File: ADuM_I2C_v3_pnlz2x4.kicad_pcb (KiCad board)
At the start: 4 copper layers, 50 x 50 mm, 336 parts, among them J1 A, J2 B, Q1 BSS138, Q2 BSS138, Q3 BSS138, Q4 BSS138, Q5 BSS138, Q6 BSS138, Q7 BSS138, Q8 BSS138, U1 ADuM1251ARZ, U2 ADuM1201AR

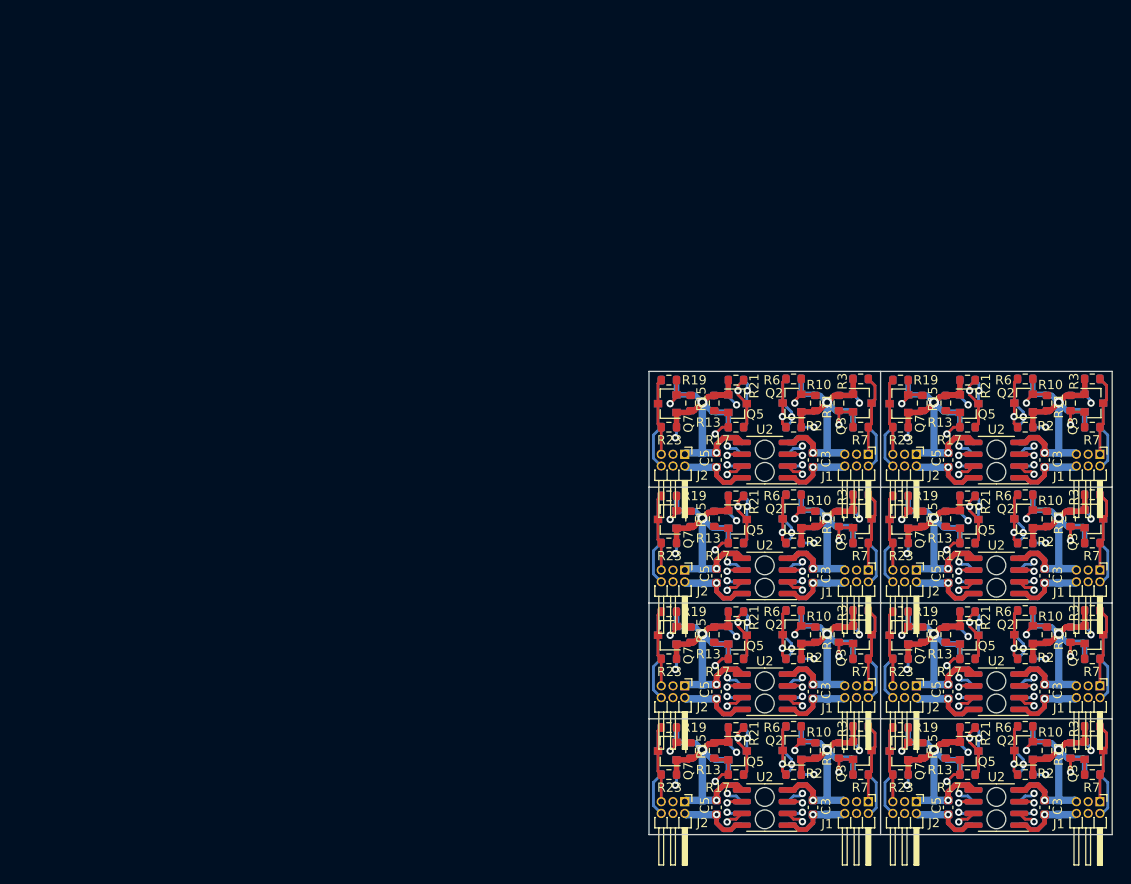
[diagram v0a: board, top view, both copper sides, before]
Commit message: Переделана панелизация платы ADuM_I2C_v3
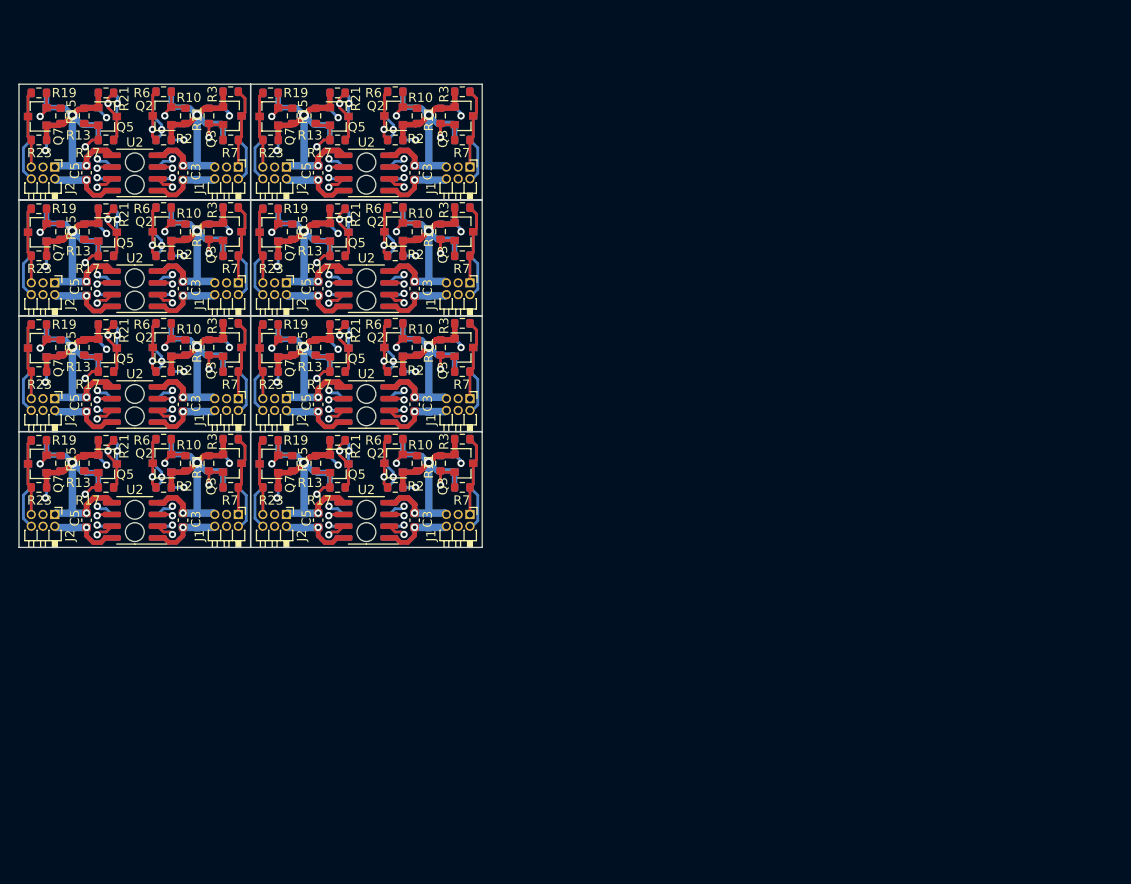
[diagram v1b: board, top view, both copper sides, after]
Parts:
- removed the C1 at (161.7, 126.6)
- removed the C1 at (136.7, 126.6)
- removed the C1 at (161.7, 114.1)
- removed the C1 at (136.7, 114.1)
- removed the C1 at (161.7, 101.6)
- removed the C1 at (136.7, 101.6)
- removed the C1 at (161.7, 89.1)
- removed the C2 at (160.2, 126.6)
- removed the C2 at (135.2, 126.6)
- removed the C2 at (160.2, 114.1)
- removed the C2 at (135.2, 114.1)
- removed the C2 at (160.2, 101.6)
- removed the C2 at (135.2, 101.6)
- removed the C2 at (160.2, 89.1)
- removed the C3 at (160.2, 126.6)
- removed the C3 at (135.2, 126.6)
- removed the C3 at (160.2, 114.1)
- removed the C3 at (135.2, 114.1)
- removed the C3 at (160.2, 101.6)
- removed the C3 at (135.2, 101.6)
- removed the C3 at (160.2, 89.1)
- removed the C4 at (149.8, 126.6)
- removed the C4 at (124.8, 126.6)
- removed the C4 at (149.8, 114.1)
- removed the C4 at (124.8, 114.1)
- removed the C4 at (149.8, 101.6)
- removed the C4 at (124.8, 101.6)
- removed the C4 at (149.8, 89.1)
- removed the C5 at (149.8, 126.6)
- removed the C5 at (124.8, 126.6)
- removed the C5 at (149.8, 114.1)
- removed the C5 at (124.8, 114.1)
- removed the C5 at (149.8, 101.6)
- removed the C5 at (124.8, 101.6)
- removed the C5 at (149.8, 89.1)
- removed the C6 at (148.3, 126.6)
- removed the C6 at (123.3, 126.6)
- removed the C6 at (148.3, 114.1)
- removed the C6 at (123.3, 114.1)
- removed the C6 at (148.3, 101.6)
- removed the C6 at (123.3, 101.6)
- removed the C6 at (148.3, 89.1)
- removed the J1 at (166.2, 125.9)
- removed the J1 at (141.2, 125.9)
- removed the J1 at (166.2, 113.4)
- removed the J1 at (141.2, 113.4)
- removed the J1 at (166.2, 100.9)
- removed the J1 at (141.2, 100.9)
- removed the J1 at (166.2, 88.4)
- removed the J2 at (146.4, 125.9)
- removed the J2 at (121.4, 125.9)
- removed the J2 at (146.4, 113.4)
- removed the J2 at (121.4, 113.4)
- removed the J2 at (146.4, 100.9)
- removed the J2 at (121.4, 100.9)
- removed the J2 at (146.4, 88.4)
- removed the Q1 at (157.9, 120.4)
- removed the Q1 at (132.9, 120.4)
- removed the Q1 at (157.9, 107.9)
- removed the Q1 at (132.9, 107.9)
- removed the Q1 at (157.9, 95.4)
- removed the Q1 at (132.9, 95.4)
- removed the Q1 at (157.9, 82.9)
- removed the Q2 at (157.9, 120.4)
- removed the Q2 at (132.9, 120.4)
- removed the Q2 at (157.9, 107.9)
- removed the Q2 at (132.9, 107.9)
- removed the Q2 at (157.9, 95.4)
- removed the Q2 at (132.9, 95.4)
- removed the Q2 at (157.9, 82.9)
- removed the Q3 at (165.5, 120.4)
- removed the Q3 at (140.5, 120.4)
- removed the Q3 at (165.5, 107.9)
- removed the Q3 at (140.5, 107.9)
- removed the Q3 at (165.5, 95.4)
- removed the Q3 at (140.5, 95.4)
- removed the Q3 at (165.5, 82.9)
- removed the Q4 at (165.5, 120.4)
- removed the Q4 at (140.5, 120.4)
- removed the Q4 at (165.5, 107.9)
- removed the Q4 at (140.5, 107.9)
- removed the Q4 at (165.5, 95.4)
- removed the Q4 at (140.5, 95.4)
- removed the Q4 at (165.5, 82.9)
- removed the Q5 at (152.1, 120.5)
- removed the Q5 at (127.1, 120.5)
- removed the Q5 at (152.1, 108.0)
- removed the Q5 at (127.1, 108.0)
- removed the Q5 at (152.1, 95.5)
- removed the Q5 at (127.1, 95.5)
- removed the Q5 at (152.1, 83.0)
- removed the Q6 at (152.1, 120.5)
- removed the Q6 at (127.1, 120.5)
- removed the Q6 at (152.1, 108.0)
- removed the Q6 at (127.1, 108.0)
- removed the Q6 at (152.1, 95.5)
- removed the Q6 at (127.1, 95.5)
- removed the Q6 at (152.1, 83.0)
- removed the Q7 at (144.5, 120.5)
- removed the Q7 at (119.5, 120.5)
- removed the Q7 at (144.5, 108.0)
- removed the Q7 at (119.5, 108.0)
- removed the Q7 at (144.5, 95.5)
- removed the Q7 at (119.5, 95.5)
- removed the Q7 at (144.5, 83.0)
- removed the Q8 at (144.5, 120.5)
- removed the Q8 at (119.5, 120.5)
- removed the Q8 at (144.5, 108.0)
- removed the Q8 at (119.5, 108.0)
- removed the Q8 at (144.5, 95.5)
- removed the Q8 at (119.5, 95.5)
- removed the Q8 at (144.5, 83.0)
- removed the R1 at (158.1, 117.8)
- removed the R1 at (133.1, 117.8)
- removed the R1 at (158.1, 105.3)
- removed the R1 at (133.1, 105.3)
- removed the R1 at (158.1, 92.8)
- removed the R1 at (133.1, 92.8)
- removed the R1 at (158.1, 80.3)
- removed the R10 at (160.5, 120.4)
- removed the R10 at (135.5, 120.4)
- removed the R10 at (160.5, 107.9)
- removed the R10 at (135.5, 107.9)
- removed the R10 at (160.5, 95.4)
- removed the R10 at (135.5, 95.4)
- removed the R10 at (160.5, 82.9)
- removed the R11 at (163.0, 120.4)
- removed the R11 at (138.0, 120.4)
- removed the R11 at (163.0, 107.9)
- removed the R11 at (138.0, 107.9)
- removed the R11 at (163.0, 95.4)
- removed the R11 at (138.0, 95.4)
- removed the R11 at (163.0, 82.9)
- removed the R12 at (163.0, 120.4)
- removed the R12 at (138.0, 120.4)
- removed the R12 at (163.0, 107.9)
- removed the R12 at (138.0, 107.9)
- removed the R12 at (163.0, 95.4)
- removed the R12 at (138.0, 95.4)
- removed the R12 at (163.0, 82.9)
- removed the R13 at (149.5, 120.4)
- removed the R13 at (124.5, 120.4)
- removed the R13 at (149.5, 107.9)
- removed the R13 at (124.5, 107.9)
- removed the R13 at (149.5, 95.4)
- removed the R13 at (124.5, 95.4)
- removed the R13 at (149.5, 82.9)
- removed the R14 at (149.5, 120.4)
- removed the R14 at (124.5, 120.4)
- removed the R14 at (149.5, 107.9)
- removed the R14 at (124.5, 107.9)
- removed the R14 at (149.5, 95.4)
- removed the R14 at (124.5, 95.4)
- removed the R14 at (149.5, 82.9)
- removed the R15 at (147.0, 120.4)
- removed the R15 at (122.0, 120.4)
- removed the R15 at (147.0, 107.9)
- removed the R15 at (122.0, 107.9)
- removed the R15 at (147.0, 95.4)
- removed the R15 at (122.0, 95.4)
- removed the R15 at (147.0, 82.9)
- removed the R16 at (147.0, 120.4)
- removed the R16 at (122.0, 120.4)
- removed the R16 at (147.0, 107.9)
- removed the R16 at (122.0, 107.9)
- removed the R16 at (147.0, 95.4)
- removed the R16 at (122.0, 95.4)
- removed the R16 at (147.0, 82.9)
- removed the R17 at (151.9, 123.0)
- removed the R17 at (126.9, 123.0)
- removed the R17 at (151.9, 110.5)
- removed the R17 at (126.9, 110.5)
- removed the R17 at (151.9, 98.0)
- removed the R17 at (126.9, 98.0)
- removed the R17 at (151.9, 85.5)
- removed the R18 at (151.9, 117.9)
- removed the R18 at (126.9, 117.9)
- removed the R18 at (151.9, 105.4)
- removed the R18 at (126.9, 105.4)
- removed the R18 at (151.9, 92.9)
- removed the R18 at (126.9, 92.9)
- removed the R18 at (151.9, 80.4)
- removed the R19 at (144.6, 117.9)
- removed the R19 at (119.6, 117.9)
- removed the R19 at (144.6, 105.4)
- removed the R19 at (119.6, 105.4)
- removed the R19 at (144.6, 92.9)
- removed the R19 at (119.6, 92.9)
- removed the R19 at (144.6, 80.4)
- removed the R2 at (158.1, 123.0)
- removed the R2 at (133.1, 123.0)
- removed the R2 at (158.1, 110.5)
- removed the R2 at (133.1, 110.5)
- removed the R2 at (158.1, 98.0)
- removed the R2 at (133.1, 98.0)
- removed the R2 at (158.1, 85.5)
- removed the R20 at (144.7, 123.0)
- removed the R20 at (119.7, 123.0)
- removed the R20 at (144.7, 110.5)
- removed the R20 at (119.7, 110.5)
- removed the R20 at (144.7, 98.0)
- removed the R20 at (119.7, 98.0)
- removed the R20 at (144.7, 85.5)
- removed the R21 at (151.9, 117.9)
- removed the R21 at (126.9, 117.9)
- removed the R21 at (151.9, 105.4)
- removed the R21 at (126.9, 105.4)
- removed the R21 at (151.9, 92.9)
- removed the R21 at (126.9, 92.9)
- removed the R21 at (151.9, 80.4)
- removed the R22 at (151.9, 123.0)
- removed the R22 at (126.9, 123.0)
- removed the R22 at (151.9, 110.5)
- removed the R22 at (126.9, 110.5)
- removed the R22 at (151.9, 98.0)
- removed the R22 at (126.9, 98.0)
- removed the R22 at (151.9, 85.5)
- removed the R23 at (144.7, 123.0)
- removed the R23 at (119.7, 123.0)
- removed the R23 at (144.7, 110.5)
- removed the R23 at (119.7, 110.5)
- removed the R23 at (144.7, 98.0)
- removed the R23 at (119.7, 98.0)
- removed the R23 at (144.7, 85.5)
- removed the R24 at (144.7, 117.9)
- removed the R24 at (119.7, 117.9)
- removed the R24 at (144.7, 105.4)
- removed the R24 at (119.7, 105.4)
- removed the R24 at (144.7, 92.9)
- removed the R24 at (119.7, 92.9)
- removed the R24 at (144.7, 80.4)
- removed the R3 at (165.3, 117.8)
- removed the R3 at (140.3, 117.8)
- removed the R3 at (165.3, 105.3)
- removed the R3 at (140.3, 105.3)
- removed the R3 at (165.3, 92.8)
- removed the R3 at (140.3, 92.8)
- removed the R3 at (165.3, 80.3)
- removed the R4 at (165.3, 123.0)
- removed the R4 at (140.3, 123.0)
- removed the R4 at (165.3, 110.5)
- removed the R4 at (140.3, 110.5)
- removed the R4 at (165.3, 98.0)
- removed the R4 at (140.3, 98.0)
- removed the R4 at (165.3, 85.5)
- removed the R5 at (158.1, 123.0)
- removed the R5 at (133.1, 123.0)
- removed the R5 at (158.1, 110.5)
- removed the R5 at (133.1, 110.5)
- removed the R5 at (158.1, 98.0)
- removed the R5 at (133.1, 98.0)
- removed the R5 at (158.1, 85.5)
- removed the R6 at (158.1, 117.8)
- removed the R6 at (133.1, 117.8)
- removed the R6 at (158.1, 105.3)
- removed the R6 at (133.1, 105.3)
- removed the R6 at (158.1, 92.8)
- removed the R6 at (133.1, 92.8)
- removed the R6 at (158.1, 80.3)
- removed the R7 at (165.4, 123.0)
- removed the R7 at (140.4, 123.0)
- removed the R7 at (165.4, 110.5)
- removed the R7 at (140.4, 110.5)
- removed the R7 at (165.4, 98.0)
- removed the R7 at (140.4, 98.0)
- removed the R7 at (165.4, 85.5)
- removed the R8 at (165.4, 117.8)
- removed the R8 at (140.4, 117.8)
- removed the R8 at (165.4, 105.3)
- removed the R8 at (140.4, 105.3)
- removed the R8 at (165.4, 92.8)
- removed the R8 at (140.4, 92.8)
- removed the R8 at (165.4, 80.3)
- removed the R9 at (160.5, 120.4)
- removed the R9 at (135.5, 120.4)
- removed the R9 at (160.5, 107.9)
- removed the R9 at (135.5, 107.9)
- removed the R9 at (160.5, 95.4)
- removed the R9 at (135.5, 95.4)
- removed the R9 at (160.5, 82.9)
- removed the U1 at (155.0, 126.6)
- removed the U1 at (130.0, 126.6)
- removed the U1 at (155.0, 114.1)
- removed the U1 at (130.0, 114.1)
- removed the U1 at (155.0, 101.6)
- removed the U1 at (130.0, 101.6)
- removed the U1 at (155.0, 89.1)
- removed the U2 at (155.0, 126.6)
- removed the U2 at (130.0, 126.6)
- removed the U2 at (155.0, 114.1)
- removed the U2 at (130.0, 114.1)
- removed the U2 at (155.0, 101.6)
- removed the U2 at (130.0, 101.6)
- removed the U2 at (155.0, 89.1)
- added C1: 1uF, Capacitor_SMD:C_0603_1608Metric, B.Cu at (93.7, 95.6)
- added C1: 1uF, Capacitor_SMD:C_0603_1608Metric, B.Cu at (68.7, 95.6)
- added C1: 1uF, Capacitor_SMD:C_0603_1608Metric, B.Cu at (93.7, 83.1)
- added C1: 1uF, Capacitor_SMD:C_0603_1608Metric, B.Cu at (68.7, 83.1)
- added C1: 1uF, Capacitor_SMD:C_0603_1608Metric, B.Cu at (93.7, 70.6)
- added C1: 1uF, Capacitor_SMD:C_0603_1608Metric, B.Cu at (68.7, 70.6)
- added C1: 1uF, Capacitor_SMD:C_0603_1608Metric, B.Cu at (93.7, 58.1)
- added C2: 100nF, Capacitor_SMD:C_0603_1608Metric, B.Cu at (92.2, 95.6)
- added C2: 100nF, Capacitor_SMD:C_0603_1608Metric, B.Cu at (67.2, 95.6)
- added C2: 100nF, Capacitor_SMD:C_0603_1608Metric, B.Cu at (92.2, 83.1)
- added C2: 100nF, Capacitor_SMD:C_0603_1608Metric, B.Cu at (67.2, 83.1)
- added C2: 100nF, Capacitor_SMD:C_0603_1608Metric, B.Cu at (92.2, 70.6)
- added C2: 100nF, Capacitor_SMD:C_0603_1608Metric, B.Cu at (67.2, 70.6)
- added C2: 100nF, Capacitor_SMD:C_0603_1608Metric, B.Cu at (92.2, 58.1)
- added C3: 100nF, Capacitor_SMD:C_0603_1608Metric, F.Cu at (92.2, 95.6)
- added C3: 100nF, Capacitor_SMD:C_0603_1608Metric, F.Cu at (67.2, 95.6)
- added C3: 100nF, Capacitor_SMD:C_0603_1608Metric, F.Cu at (92.2, 83.1)
- added C3: 100nF, Capacitor_SMD:C_0603_1608Metric, F.Cu at (67.2, 83.1)
- added C3: 100nF, Capacitor_SMD:C_0603_1608Metric, F.Cu at (92.2, 70.6)
- added C3: 100nF, Capacitor_SMD:C_0603_1608Metric, F.Cu at (67.2, 70.6)
- added C3: 100nF, Capacitor_SMD:C_0603_1608Metric, F.Cu at (92.2, 58.1)
- added C4: 100nF, Capacitor_SMD:C_0603_1608Metric, B.Cu at (81.8, 95.6)
- added C4: 100nF, Capacitor_SMD:C_0603_1608Metric, B.Cu at (56.8, 95.6)
- added C4: 100nF, Capacitor_SMD:C_0603_1608Metric, B.Cu at (81.8, 83.1)
- added C4: 100nF, Capacitor_SMD:C_0603_1608Metric, B.Cu at (56.8, 83.1)
- added C4: 100nF, Capacitor_SMD:C_0603_1608Metric, B.Cu at (81.8, 70.6)
- added C4: 100nF, Capacitor_SMD:C_0603_1608Metric, B.Cu at (56.8, 70.6)
- added C4: 100nF, Capacitor_SMD:C_0603_1608Metric, B.Cu at (81.8, 58.1)
- added C5: 100nF, Capacitor_SMD:C_0603_1608Metric, F.Cu at (81.8, 95.6)
- added C5: 100nF, Capacitor_SMD:C_0603_1608Metric, F.Cu at (56.8, 95.6)
- added C5: 100nF, Capacitor_SMD:C_0603_1608Metric, F.Cu at (81.8, 83.1)
- added C5: 100nF, Capacitor_SMD:C_0603_1608Metric, F.Cu at (56.8, 83.1)
- added C5: 100nF, Capacitor_SMD:C_0603_1608Metric, F.Cu at (81.8, 70.6)
- added C5: 100nF, Capacitor_SMD:C_0603_1608Metric, F.Cu at (56.8, 70.6)
- added C5: 100nF, Capacitor_SMD:C_0603_1608Metric, F.Cu at (81.8, 58.1)
- added C6: 1uF, Capacitor_SMD:C_0603_1608Metric, B.Cu at (80.3, 95.6)
- added C6: 1uF, Capacitor_SMD:C_0603_1608Metric, B.Cu at (55.3, 95.6)
- added C6: 1uF, Capacitor_SMD:C_0603_1608Metric, B.Cu at (80.3, 83.1)
- added C6: 1uF, Capacitor_SMD:C_0603_1608Metric, B.Cu at (55.3, 83.1)
- added C6: 1uF, Capacitor_SMD:C_0603_1608Metric, B.Cu at (80.3, 70.6)
- added C6: 1uF, Capacitor_SMD:C_0603_1608Metric, B.Cu at (55.3, 70.6)
- added C6: 1uF, Capacitor_SMD:C_0603_1608Metric, B.Cu at (80.3, 58.1)
- added J1: A, Modules:PinHeader_2x03_P1.27mm_Horizontal_short, F.Cu at (98.2, 94.9)
- added J1: A, Modules:PinHeader_2x03_P1.27mm_Horizontal_short, F.Cu at (73.2, 94.9)
- added J1: A, Modules:PinHeader_2x03_P1.27mm_Horizontal_short, F.Cu at (98.2, 82.4)
- added J1: A, Modules:PinHeader_2x03_P1.27mm_Horizontal_short, F.Cu at (73.2, 82.4)
- added J1: A, Modules:PinHeader_2x03_P1.27mm_Horizontal_short, F.Cu at (98.2, 69.9)
- added J1: A, Modules:PinHeader_2x03_P1.27mm_Horizontal_short, F.Cu at (73.2, 69.9)
- added J1: A, Modules:PinHeader_2x03_P1.27mm_Horizontal_short, F.Cu at (98.2, 57.4)
- added J2: B, Modules:PinHeader_2x03_P1.27mm_Horizontal_short, F.Cu at (78.4, 94.9)
- added J2: B, Modules:PinHeader_2x03_P1.27mm_Horizontal_short, F.Cu at (53.4, 94.9)
- added J2: B, Modules:PinHeader_2x03_P1.27mm_Horizontal_short, F.Cu at (78.4, 82.4)
- added J2: B, Modules:PinHeader_2x03_P1.27mm_Horizontal_short, F.Cu at (53.4, 82.4)
- added J2: B, Modules:PinHeader_2x03_P1.27mm_Horizontal_short, F.Cu at (78.4, 69.9)
- added J2: B, Modules:PinHeader_2x03_P1.27mm_Horizontal_short, F.Cu at (53.4, 69.9)
- added J2: B, Modules:PinHeader_2x03_P1.27mm_Horizontal_short, F.Cu at (78.4, 57.4)
- added Q1: BSS138, Package_TO_SOT_SMD:SOT-23, B.Cu at (89.9, 89.4)
- added Q1: BSS138, Package_TO_SOT_SMD:SOT-23, B.Cu at (64.9, 89.4)
- added Q1: BSS138, Package_TO_SOT_SMD:SOT-23, B.Cu at (89.9, 76.9)
- added Q1: BSS138, Package_TO_SOT_SMD:SOT-23, B.Cu at (64.9, 76.9)
- added Q1: BSS138, Package_TO_SOT_SMD:SOT-23, B.Cu at (89.9, 64.4)
- added Q1: BSS138, Package_TO_SOT_SMD:SOT-23, B.Cu at (64.9, 64.4)
- added Q1: BSS138, Package_TO_SOT_SMD:SOT-23, B.Cu at (89.9, 51.9)
- added Q2: BSS138, Package_TO_SOT_SMD:SOT-23, F.Cu at (89.9, 89.4)
- added Q2: BSS138, Package_TO_SOT_SMD:SOT-23, F.Cu at (64.9, 89.4)
- added Q2: BSS138, Package_TO_SOT_SMD:SOT-23, F.Cu at (89.9, 76.9)
- added Q2: BSS138, Package_TO_SOT_SMD:SOT-23, F.Cu at (64.9, 76.9)
- added Q2: BSS138, Package_TO_SOT_SMD:SOT-23, F.Cu at (89.9, 64.4)
- added Q2: BSS138, Package_TO_SOT_SMD:SOT-23, F.Cu at (64.9, 64.4)
- added Q2: BSS138, Package_TO_SOT_SMD:SOT-23, F.Cu at (89.9, 51.9)
- added Q3: BSS138, Package_TO_SOT_SMD:SOT-23, F.Cu at (97.5, 89.4)
- added Q3: BSS138, Package_TO_SOT_SMD:SOT-23, F.Cu at (72.5, 89.4)
- added Q3: BSS138, Package_TO_SOT_SMD:SOT-23, F.Cu at (97.5, 76.9)
- added Q3: BSS138, Package_TO_SOT_SMD:SOT-23, F.Cu at (72.5, 76.9)
- added Q3: BSS138, Package_TO_SOT_SMD:SOT-23, F.Cu at (97.5, 64.4)
- added Q3: BSS138, Package_TO_SOT_SMD:SOT-23, F.Cu at (72.5, 64.4)
- added Q3: BSS138, Package_TO_SOT_SMD:SOT-23, F.Cu at (97.5, 51.9)
- added Q4: BSS138, Package_TO_SOT_SMD:SOT-23, B.Cu at (97.5, 89.4)
- added Q4: BSS138, Package_TO_SOT_SMD:SOT-23, B.Cu at (72.5, 89.4)
- added Q4: BSS138, Package_TO_SOT_SMD:SOT-23, B.Cu at (97.5, 76.9)
- added Q4: BSS138, Package_TO_SOT_SMD:SOT-23, B.Cu at (72.5, 76.9)
- added Q4: BSS138, Package_TO_SOT_SMD:SOT-23, B.Cu at (97.5, 64.4)
- added Q4: BSS138, Package_TO_SOT_SMD:SOT-23, B.Cu at (72.5, 64.4)
- added Q4: BSS138, Package_TO_SOT_SMD:SOT-23, B.Cu at (97.5, 51.9)
- added Q5: BSS138, Package_TO_SOT_SMD:SOT-23, F.Cu at (84.1, 89.5)
- added Q5: BSS138, Package_TO_SOT_SMD:SOT-23, F.Cu at (59.1, 89.5)
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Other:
- outline, holes or cut-outs redrawn

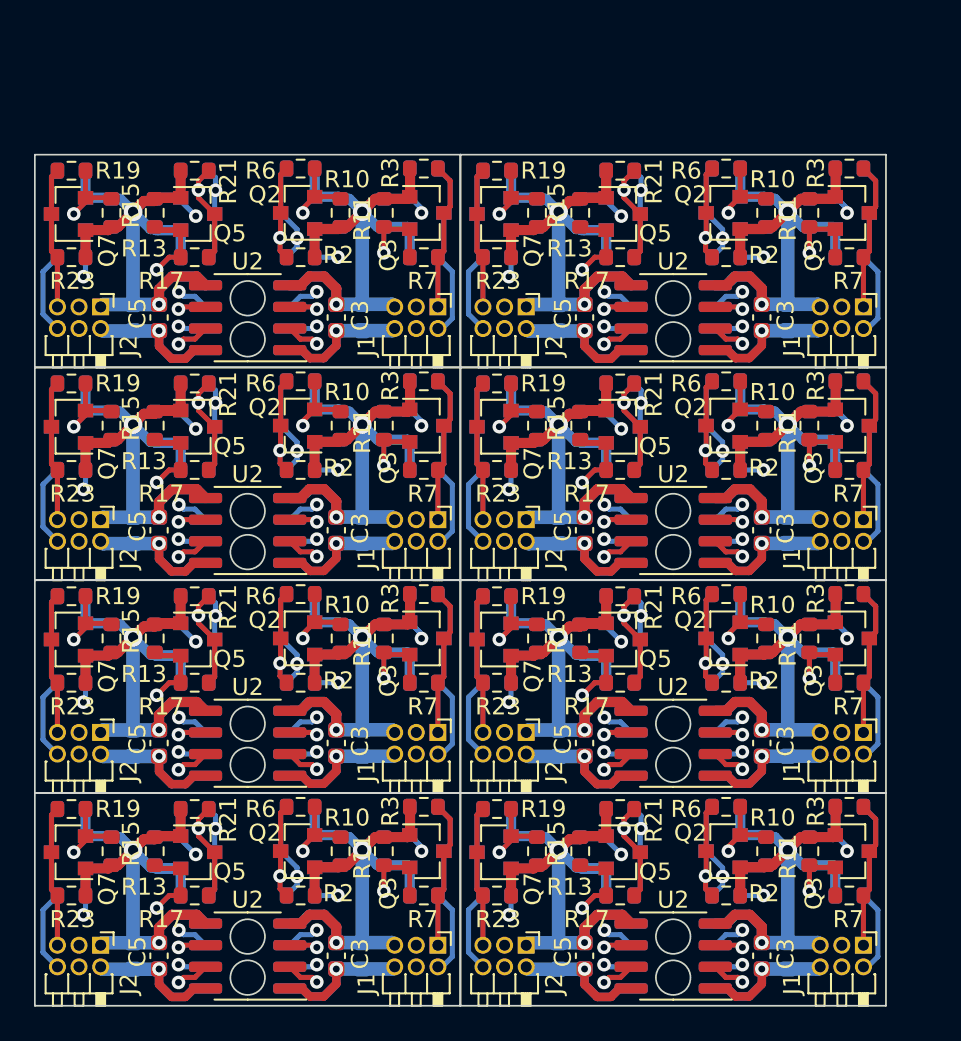
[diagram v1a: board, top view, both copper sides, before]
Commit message: Созданы две панели: односторонняя и двухсторонняя, объединяющие все платы, кроме цифрового модуля. Добавлен окантовка по контуру платы с двух сторон и текст: "JLCJLCJLCJLC"
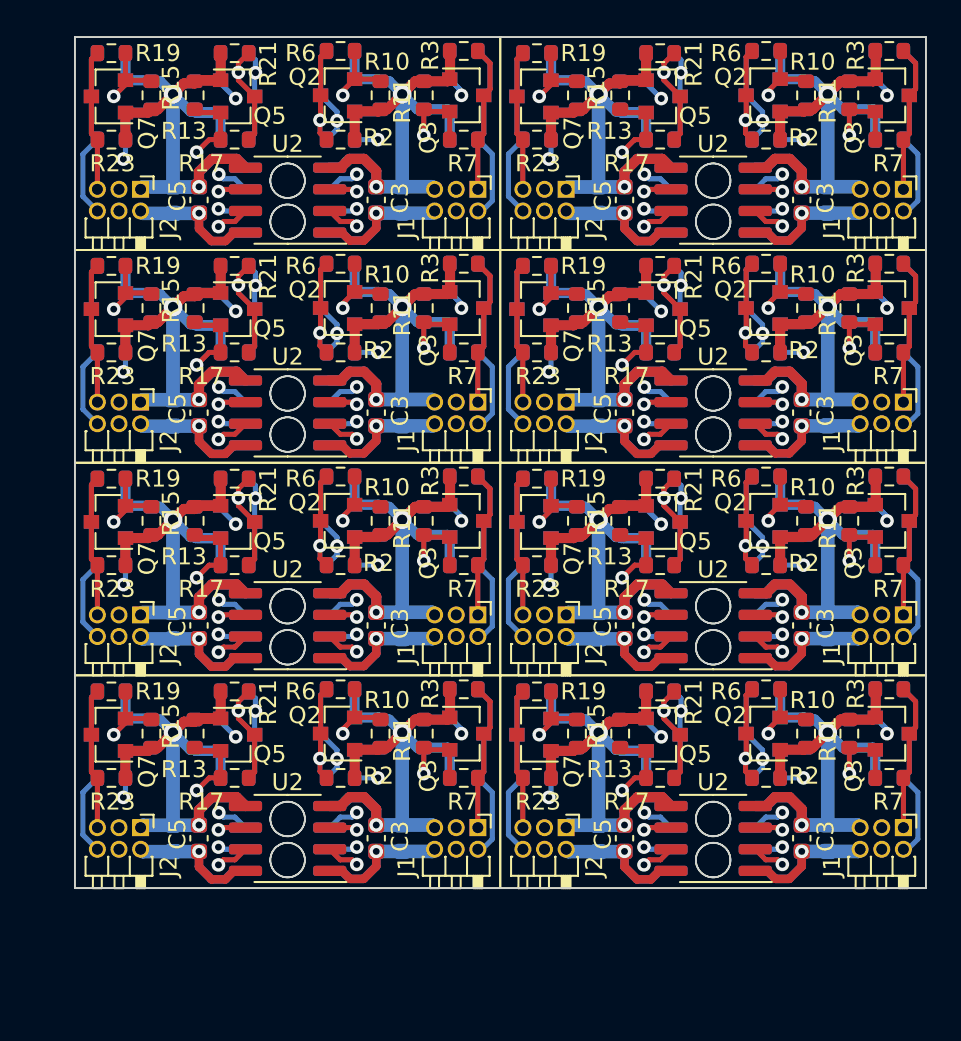
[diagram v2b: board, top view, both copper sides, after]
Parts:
- removed the C1 at (93.7, 95.6)
- removed the C1 at (68.7, 95.6)
- removed the C1 at (93.7, 83.1)
- removed the C1 at (68.7, 83.1)
- removed the C1 at (93.7, 70.6)
- removed the C1 at (68.7, 70.6)
- removed the C1 at (93.7, 58.1)
- removed the C2 at (92.2, 95.6)
- removed the C2 at (67.2, 95.6)
- removed the C2 at (92.2, 83.1)
- removed the C2 at (67.2, 83.1)
- removed the C2 at (92.2, 70.6)
- removed the C2 at (67.2, 70.6)
- removed the C2 at (92.2, 58.1)
- removed the C3 at (92.2, 95.6)
- removed the C3 at (67.2, 95.6)
- removed the C3 at (92.2, 83.1)
- removed the C3 at (67.2, 83.1)
- removed the C3 at (92.2, 70.6)
- removed the C3 at (67.2, 70.6)
- removed the C3 at (92.2, 58.1)
- removed the C4 at (81.8, 95.6)
- removed the C4 at (56.8, 95.6)
- removed the C4 at (81.8, 83.1)
- removed the C4 at (56.8, 83.1)
- removed the C4 at (81.8, 70.6)
- removed the C4 at (56.8, 70.6)
- removed the C4 at (81.8, 58.1)
- removed the C5 at (81.8, 95.6)
- removed the C5 at (56.8, 95.6)
- removed the C5 at (81.8, 83.1)
- removed the C5 at (56.8, 83.1)
- removed the C5 at (81.8, 70.6)
- removed the C5 at (56.8, 70.6)
- removed the C5 at (81.8, 58.1)
- removed the C6 at (80.3, 95.6)
- removed the C6 at (55.3, 95.6)
- removed the C6 at (80.3, 83.1)
- removed the C6 at (55.3, 83.1)
- removed the C6 at (80.3, 70.6)
- removed the C6 at (55.3, 70.6)
- removed the C6 at (80.3, 58.1)
- removed the J1 at (98.2, 94.9)
- removed the J1 at (73.2, 94.9)
- removed the J1 at (98.2, 82.4)
- removed the J1 at (73.2, 82.4)
- removed the J1 at (98.2, 69.9)
- removed the J1 at (73.2, 69.9)
- removed the J1 at (98.2, 57.4)
- removed the J2 at (78.4, 94.9)
- removed the J2 at (53.4, 94.9)
- removed the J2 at (78.4, 82.4)
- removed the J2 at (53.4, 82.4)
- removed the J2 at (78.4, 69.9)
- removed the J2 at (53.4, 69.9)
- removed the J2 at (78.4, 57.4)
- removed the Q1 at (89.9, 89.4)
- removed the Q1 at (64.9, 89.4)
- removed the Q1 at (89.9, 76.9)
- removed the Q1 at (64.9, 76.9)
- removed the Q1 at (89.9, 64.4)
- removed the Q1 at (64.9, 64.4)
- removed the Q1 at (89.9, 51.9)
- removed the Q2 at (89.9, 89.4)
- removed the Q2 at (64.9, 89.4)
- removed the Q2 at (89.9, 76.9)
- removed the Q2 at (64.9, 76.9)
- removed the Q2 at (89.9, 64.4)
- removed the Q2 at (64.9, 64.4)
- removed the Q2 at (89.9, 51.9)
- removed the Q3 at (97.5, 89.4)
- removed the Q3 at (72.5, 89.4)
- removed the Q3 at (97.5, 76.9)
- removed the Q3 at (72.5, 76.9)
- removed the Q3 at (97.5, 64.4)
- removed the Q3 at (72.5, 64.4)
- removed the Q3 at (97.5, 51.9)
- removed the Q4 at (97.5, 89.4)
- removed the Q4 at (72.5, 89.4)
- removed the Q4 at (97.5, 76.9)
- removed the Q4 at (72.5, 76.9)
- removed the Q4 at (97.5, 64.4)
- removed the Q4 at (72.5, 64.4)
- removed the Q4 at (97.5, 51.9)
- removed the Q5 at (84.1, 89.5)
- removed the Q5 at (59.1, 89.5)
- removed the Q5 at (84.1, 77.0)
- removed the Q5 at (59.1, 77.0)
- removed the Q5 at (84.1, 64.5)
- removed the Q5 at (59.1, 64.5)
- removed the Q5 at (84.1, 52.0)
- removed the Q6 at (84.1, 89.5)
- removed the Q6 at (59.1, 89.5)
- removed the Q6 at (84.1, 77.0)
- removed the Q6 at (59.1, 77.0)
- removed the Q6 at (84.1, 64.5)
- removed the Q6 at (59.1, 64.5)
- removed the Q6 at (84.1, 52.0)
- removed the Q7 at (76.5, 89.5)
- removed the Q7 at (51.5, 89.5)
- removed the Q7 at (76.5, 77.0)
- removed the Q7 at (51.5, 77.0)
- removed the Q7 at (76.5, 64.5)
- removed the Q7 at (51.5, 64.5)
- removed the Q7 at (76.5, 52.0)
- removed the Q8 at (76.5, 89.5)
- removed the Q8 at (51.5, 89.5)
- removed the Q8 at (76.5, 77.0)
- removed the Q8 at (51.5, 77.0)
- removed the Q8 at (76.5, 64.5)
- removed the Q8 at (51.5, 64.5)
- removed the Q8 at (76.5, 52.0)
- removed the R1 at (90.1, 86.8)
- removed the R1 at (65.1, 86.8)
- removed the R1 at (90.1, 74.3)
- removed the R1 at (65.1, 74.3)
- removed the R1 at (90.1, 61.8)
- removed the R1 at (65.1, 61.8)
- removed the R1 at (90.1, 49.3)
- removed the R10 at (92.5, 89.4)
- removed the R10 at (67.5, 89.4)
- removed the R10 at (92.5, 76.9)
- removed the R10 at (67.5, 76.9)
- removed the R10 at (92.5, 64.4)
- removed the R10 at (67.5, 64.4)
- removed the R10 at (92.5, 51.9)
- removed the R11 at (95.0, 89.4)
- removed the R11 at (70.0, 89.4)
- removed the R11 at (95.0, 76.9)
- removed the R11 at (70.0, 76.9)
- removed the R11 at (95.0, 64.4)
- removed the R11 at (70.0, 64.4)
- removed the R11 at (95.0, 51.9)
- removed the R12 at (95.0, 89.4)
- removed the R12 at (70.0, 89.4)
- removed the R12 at (95.0, 76.9)
- removed the R12 at (70.0, 76.9)
- removed the R12 at (95.0, 64.4)
- removed the R12 at (70.0, 64.4)
- removed the R12 at (95.0, 51.9)
- removed the R13 at (81.5, 89.4)
- removed the R13 at (56.5, 89.4)
- removed the R13 at (81.5, 76.9)
- removed the R13 at (56.5, 76.9)
- removed the R13 at (81.5, 64.4)
- removed the R13 at (56.5, 64.4)
- removed the R13 at (81.5, 51.9)
- removed the R14 at (81.5, 89.4)
- removed the R14 at (56.5, 89.4)
- removed the R14 at (81.5, 76.9)
- removed the R14 at (56.5, 76.9)
- removed the R14 at (81.5, 64.4)
- removed the R14 at (56.5, 64.4)
- removed the R14 at (81.5, 51.9)
- removed the R15 at (79.0, 89.4)
- removed the R15 at (54.0, 89.4)
- removed the R15 at (79.0, 76.9)
- removed the R15 at (54.0, 76.9)
- removed the R15 at (79.0, 64.4)
- removed the R15 at (54.0, 64.4)
- removed the R15 at (79.0, 51.9)
- removed the R16 at (79.0, 89.4)
- removed the R16 at (54.0, 89.4)
- removed the R16 at (79.0, 76.9)
- removed the R16 at (54.0, 76.9)
- removed the R16 at (79.0, 64.4)
- removed the R16 at (54.0, 64.4)
- removed the R16 at (79.0, 51.9)
- removed the R17 at (83.9, 92.0)
- removed the R17 at (58.9, 92.0)
- removed the R17 at (83.9, 79.5)
- removed the R17 at (58.9, 79.5)
- removed the R17 at (83.9, 67.0)
- removed the R17 at (58.9, 67.0)
- removed the R17 at (83.9, 54.5)
- removed the R18 at (83.9, 86.9)
- removed the R18 at (58.9, 86.9)
- removed the R18 at (83.9, 74.4)
- removed the R18 at (58.9, 74.4)
- removed the R18 at (83.9, 61.9)
- removed the R18 at (58.9, 61.9)
- removed the R18 at (83.9, 49.4)
- removed the R19 at (76.6, 86.9)
- removed the R19 at (51.6, 86.9)
- removed the R19 at (76.6, 74.4)
- removed the R19 at (51.6, 74.4)
- removed the R19 at (76.6, 61.9)
- removed the R19 at (51.6, 61.9)
- removed the R19 at (76.6, 49.4)
- removed the R2 at (90.1, 92.0)
- removed the R2 at (65.1, 92.0)
- removed the R2 at (90.1, 79.5)
- removed the R2 at (65.1, 79.5)
- removed the R2 at (90.1, 67.0)
- removed the R2 at (65.1, 67.0)
- removed the R2 at (90.1, 54.5)
- removed the R20 at (76.7, 92.0)
- removed the R20 at (51.6, 92.0)
- removed the R20 at (76.7, 79.5)
- removed the R20 at (51.6, 79.5)
- removed the R20 at (76.7, 67.0)
- removed the R20 at (51.6, 67.0)
- removed the R20 at (76.7, 54.5)
- removed the R21 at (83.9, 86.9)
- removed the R21 at (58.9, 86.9)
- removed the R21 at (83.9, 74.4)
- removed the R21 at (58.9, 74.4)
- removed the R21 at (83.9, 61.9)
- removed the R21 at (58.9, 61.9)
- removed the R21 at (83.9, 49.4)
- removed the R22 at (83.9, 92.0)
- removed the R22 at (58.9, 92.0)
- removed the R22 at (83.9, 79.5)
- removed the R22 at (58.9, 79.5)
- removed the R22 at (83.9, 67.0)
- removed the R22 at (58.9, 67.0)
- removed the R22 at (83.9, 54.5)
- removed the R23 at (76.7, 92.0)
- removed the R23 at (51.6, 92.0)
- removed the R23 at (76.7, 79.5)
- removed the R23 at (51.6, 79.5)
- removed the R23 at (76.7, 67.0)
- removed the R23 at (51.6, 67.0)
- removed the R23 at (76.7, 54.5)
- removed the R24 at (76.7, 86.9)
- removed the R24 at (51.6, 86.9)
- removed the R24 at (76.7, 74.4)
- removed the R24 at (51.6, 74.4)
- removed the R24 at (76.7, 61.9)
- removed the R24 at (51.6, 61.9)
- removed the R24 at (76.7, 49.4)
- removed the R3 at (97.3, 86.8)
- removed the R3 at (72.3, 86.8)
- removed the R3 at (97.3, 74.3)
- removed the R3 at (72.3, 74.3)
- removed the R3 at (97.3, 61.8)
- removed the R3 at (72.3, 61.8)
- removed the R3 at (97.3, 49.3)
- removed the R4 at (97.3, 92.0)
- removed the R4 at (72.3, 92.0)
- removed the R4 at (97.3, 79.5)
- removed the R4 at (72.3, 79.5)
- removed the R4 at (97.3, 67.0)
- removed the R4 at (72.3, 67.0)
- removed the R4 at (97.3, 54.5)
- removed the R5 at (90.1, 92.0)
- removed the R5 at (65.1, 92.0)
- removed the R5 at (90.1, 79.5)
- removed the R5 at (65.1, 79.5)
- removed the R5 at (90.1, 67.0)
- removed the R5 at (65.1, 67.0)
- removed the R5 at (90.1, 54.5)
- removed the R6 at (90.1, 86.8)
- removed the R6 at (65.1, 86.8)
- removed the R6 at (90.1, 74.3)
- removed the R6 at (65.1, 74.3)
- removed the R6 at (90.1, 61.8)
- removed the R6 at (65.1, 61.8)
- removed the R6 at (90.1, 49.3)
- removed the R7 at (97.4, 92.0)
- removed the R7 at (72.4, 92.0)
- removed the R7 at (97.4, 79.5)
- removed the R7 at (72.4, 79.5)
- removed the R7 at (97.4, 67.0)
- removed the R7 at (72.4, 67.0)
- removed the R7 at (97.4, 54.5)
- removed the R8 at (97.4, 86.8)
- removed the R8 at (72.4, 86.8)
- removed the R8 at (97.4, 74.3)
- removed the R8 at (72.4, 74.3)
- removed the R8 at (97.4, 61.8)
- removed the R8 at (72.4, 61.8)
- removed the R8 at (97.4, 49.3)
- removed the R9 at (92.5, 89.4)
- removed the R9 at (67.5, 89.4)
- removed the R9 at (92.5, 76.9)
- removed the R9 at (67.5, 76.9)
- removed the R9 at (92.5, 64.4)
- removed the R9 at (67.5, 64.4)
- removed the R9 at (92.5, 51.9)
- removed the U1 at (87.0, 95.6)
- removed the U1 at (62.0, 95.6)
- removed the U1 at (87.0, 83.1)
- removed the U1 at (62.0, 83.1)
- removed the U1 at (87.0, 70.6)
- removed the U1 at (62.0, 70.6)
- removed the U1 at (87.0, 58.1)
- removed the U2 at (87.0, 95.6)
- removed the U2 at (62.0, 95.6)
- removed the U2 at (87.0, 83.1)
- removed the U2 at (62.0, 83.1)
- removed the U2 at (87.0, 70.6)
- removed the U2 at (62.0, 70.6)
- removed the U2 at (87.0, 58.1)
- added C1: 1uF, Capacitor_SMD:C_0603_1608Metric, B.Cu at (96.1, 88.7)
- added C1: 1uF, Capacitor_SMD:C_0603_1608Metric, B.Cu at (71.1, 88.7)
- added C1: 1uF, Capacitor_SMD:C_0603_1608Metric, B.Cu at (96.1, 76.2)
- added C1: 1uF, Capacitor_SMD:C_0603_1608Metric, B.Cu at (71.1, 76.2)
- added C1: 1uF, Capacitor_SMD:C_0603_1608Metric, B.Cu at (96.1, 63.7)
- added C1: 1uF, Capacitor_SMD:C_0603_1608Metric, B.Cu at (71.1, 63.7)
- added C1: 1uF, Capacitor_SMD:C_0603_1608Metric, B.Cu at (96.1, 51.2)
- added C2: 100nF, Capacitor_SMD:C_0603_1608Metric, B.Cu at (94.6, 88.7)
- added C2: 100nF, Capacitor_SMD:C_0603_1608Metric, B.Cu at (69.6, 88.7)
- added C2: 100nF, Capacitor_SMD:C_0603_1608Metric, B.Cu at (94.6, 76.2)
- added C2: 100nF, Capacitor_SMD:C_0603_1608Metric, B.Cu at (69.6, 76.2)
- added C2: 100nF, Capacitor_SMD:C_0603_1608Metric, B.Cu at (94.6, 63.7)
- added C2: 100nF, Capacitor_SMD:C_0603_1608Metric, B.Cu at (69.6, 63.7)
- added C2: 100nF, Capacitor_SMD:C_0603_1608Metric, B.Cu at (94.6, 51.2)
- added C3: 100nF, Capacitor_SMD:C_0603_1608Metric, F.Cu at (94.6, 88.7)
- added C3: 100nF, Capacitor_SMD:C_0603_1608Metric, F.Cu at (69.6, 88.7)
- added C3: 100nF, Capacitor_SMD:C_0603_1608Metric, F.Cu at (94.6, 76.2)
- added C3: 100nF, Capacitor_SMD:C_0603_1608Metric, F.Cu at (69.6, 76.2)
- added C3: 100nF, Capacitor_SMD:C_0603_1608Metric, F.Cu at (94.6, 63.7)
- added C3: 100nF, Capacitor_SMD:C_0603_1608Metric, F.Cu at (69.6, 63.7)
- added C3: 100nF, Capacitor_SMD:C_0603_1608Metric, F.Cu at (94.6, 51.2)
- added C4: 100nF, Capacitor_SMD:C_0603_1608Metric, B.Cu at (84.1, 88.7)
- added C4: 100nF, Capacitor_SMD:C_0603_1608Metric, B.Cu at (59.1, 88.7)
- added C4: 100nF, Capacitor_SMD:C_0603_1608Metric, B.Cu at (84.1, 76.2)
- added C4: 100nF, Capacitor_SMD:C_0603_1608Metric, B.Cu at (59.1, 76.2)
- added C4: 100nF, Capacitor_SMD:C_0603_1608Metric, B.Cu at (84.1, 63.7)
- added C4: 100nF, Capacitor_SMD:C_0603_1608Metric, B.Cu at (59.1, 63.7)
- added C4: 100nF, Capacitor_SMD:C_0603_1608Metric, B.Cu at (84.1, 51.2)
- added C5: 100nF, Capacitor_SMD:C_0603_1608Metric, F.Cu at (84.1, 88.7)
- added C5: 100nF, Capacitor_SMD:C_0603_1608Metric, F.Cu at (59.1, 88.7)
- added C5: 100nF, Capacitor_SMD:C_0603_1608Metric, F.Cu at (84.1, 76.2)
- added C5: 100nF, Capacitor_SMD:C_0603_1608Metric, F.Cu at (59.1, 76.2)
- added C5: 100nF, Capacitor_SMD:C_0603_1608Metric, F.Cu at (84.1, 63.7)
- added C5: 100nF, Capacitor_SMD:C_0603_1608Metric, F.Cu at (59.1, 63.7)
- added C5: 100nF, Capacitor_SMD:C_0603_1608Metric, F.Cu at (84.1, 51.2)
- added C6: 1uF, Capacitor_SMD:C_0603_1608Metric, B.Cu at (82.6, 88.7)
- added C6: 1uF, Capacitor_SMD:C_0603_1608Metric, B.Cu at (57.6, 88.7)
- added C6: 1uF, Capacitor_SMD:C_0603_1608Metric, B.Cu at (82.6, 76.2)
- added C6: 1uF, Capacitor_SMD:C_0603_1608Metric, B.Cu at (57.6, 76.2)
- added C6: 1uF, Capacitor_SMD:C_0603_1608Metric, B.Cu at (82.6, 63.7)
- added C6: 1uF, Capacitor_SMD:C_0603_1608Metric, B.Cu at (57.6, 63.7)
- added C6: 1uF, Capacitor_SMD:C_0603_1608Metric, B.Cu at (82.6, 51.2)
- added J1: A, Modules:PinHeader_2x03_P1.27mm_Horizontal_short, F.Cu at (100.5, 88.0)
- added J1: A, Modules:PinHeader_2x03_P1.27mm_Horizontal_short, F.Cu at (75.5, 88.0)
- added J1: A, Modules:PinHeader_2x03_P1.27mm_Horizontal_short, F.Cu at (100.5, 75.5)
- added J1: A, Modules:PinHeader_2x03_P1.27mm_Horizontal_short, F.Cu at (75.5, 75.5)
- added J1: A, Modules:PinHeader_2x03_P1.27mm_Horizontal_short, F.Cu at (100.5, 63.0)
- added J1: A, Modules:PinHeader_2x03_P1.27mm_Horizontal_short, F.Cu at (75.5, 63.0)
- added J1: A, Modules:PinHeader_2x03_P1.27mm_Horizontal_short, F.Cu at (100.5, 50.5)
- added J2: B, Modules:PinHeader_2x03_P1.27mm_Horizontal_short, F.Cu at (80.7, 88.0)
- added J2: B, Modules:PinHeader_2x03_P1.27mm_Horizontal_short, F.Cu at (55.7, 88.0)
- added J2: B, Modules:PinHeader_2x03_P1.27mm_Horizontal_short, F.Cu at (80.7, 75.5)
- added J2: B, Modules:PinHeader_2x03_P1.27mm_Horizontal_short, F.Cu at (55.7, 75.5)
- added J2: B, Modules:PinHeader_2x03_P1.27mm_Horizontal_short, F.Cu at (80.7, 63.0)
- added J2: B, Modules:PinHeader_2x03_P1.27mm_Horizontal_short, F.Cu at (55.7, 63.0)
- added J2: B, Modules:PinHeader_2x03_P1.27mm_Horizontal_short, F.Cu at (80.7, 50.5)
- added Q1: BSS138, Package_TO_SOT_SMD:SOT-23, B.Cu at (92.3, 82.5)
- added Q1: BSS138, Package_TO_SOT_SMD:SOT-23, B.Cu at (67.3, 82.5)
- added Q1: BSS138, Package_TO_SOT_SMD:SOT-23, B.Cu at (92.3, 70.0)
- added Q1: BSS138, Package_TO_SOT_SMD:SOT-23, B.Cu at (67.3, 70.0)
- added Q1: BSS138, Package_TO_SOT_SMD:SOT-23, B.Cu at (92.3, 57.5)
- added Q1: BSS138, Package_TO_SOT_SMD:SOT-23, B.Cu at (67.3, 57.5)
- added Q1: BSS138, Package_TO_SOT_SMD:SOT-23, B.Cu at (92.3, 45.0)
- added Q2: BSS138, Package_TO_SOT_SMD:SOT-23, F.Cu at (92.3, 82.5)
- added Q2: BSS138, Package_TO_SOT_SMD:SOT-23, F.Cu at (67.3, 82.5)
- added Q2: BSS138, Package_TO_SOT_SMD:SOT-23, F.Cu at (92.3, 70.0)
- added Q2: BSS138, Package_TO_SOT_SMD:SOT-23, F.Cu at (67.3, 70.0)
- added Q2: BSS138, Package_TO_SOT_SMD:SOT-23, F.Cu at (92.3, 57.5)
- added Q2: BSS138, Package_TO_SOT_SMD:SOT-23, F.Cu at (67.3, 57.5)
- added Q2: BSS138, Package_TO_SOT_SMD:SOT-23, F.Cu at (92.3, 45.0)
- added Q3: BSS138, Package_TO_SOT_SMD:SOT-23, F.Cu at (99.9, 82.5)
- added Q3: BSS138, Package_TO_SOT_SMD:SOT-23, F.Cu at (74.9, 82.5)
- added Q3: BSS138, Package_TO_SOT_SMD:SOT-23, F.Cu at (99.9, 70.0)
- added Q3: BSS138, Package_TO_SOT_SMD:SOT-23, F.Cu at (74.9, 70.0)
- added Q3: BSS138, Package_TO_SOT_SMD:SOT-23, F.Cu at (99.9, 57.5)
- added Q3: BSS138, Package_TO_SOT_SMD:SOT-23, F.Cu at (74.9, 57.5)
- added Q3: BSS138, Package_TO_SOT_SMD:SOT-23, F.Cu at (99.9, 45.0)
- added Q4: BSS138, Package_TO_SOT_SMD:SOT-23, B.Cu at (99.9, 82.5)
- added Q4: BSS138, Package_TO_SOT_SMD:SOT-23, B.Cu at (74.9, 82.5)
- added Q4: BSS138, Package_TO_SOT_SMD:SOT-23, B.Cu at (99.9, 70.0)
- added Q4: BSS138, Package_TO_SOT_SMD:SOT-23, B.Cu at (74.9, 70.0)
- added Q4: BSS138, Package_TO_SOT_SMD:SOT-23, B.Cu at (99.9, 57.5)
- added Q4: BSS138, Package_TO_SOT_SMD:SOT-23, B.Cu at (74.9, 57.5)
- added Q4: BSS138, Package_TO_SOT_SMD:SOT-23, B.Cu at (99.9, 45.0)
- added Q5: BSS138, Package_TO_SOT_SMD:SOT-23, F.Cu at (86.4, 82.6)
- added Q5: BSS138, Package_TO_SOT_SMD:SOT-23, F.Cu at (61.4, 82.6)
- added Q5: BSS138, Package_TO_SOT_SMD:SOT-23, F.Cu at (86.4, 70.1)
- added Q5: BSS138, Package_TO_SOT_SMD:SOT-23, F.Cu at (61.4, 70.1)
- added Q5: BSS138, Package_TO_SOT_SMD:SOT-23, F.Cu at (86.4, 57.6)
- added Q5: BSS138, Package_TO_SOT_SMD:SOT-23, F.Cu at (61.4, 57.6)
- added Q5: BSS138, Package_TO_SOT_SMD:SOT-23, F.Cu at (86.4, 45.1)
- added Q6: BSS138, Package_TO_SOT_SMD:SOT-23, B.Cu at (86.4, 82.6)
- added Q6: BSS138, Package_TO_SOT_SMD:SOT-23, B.Cu at (61.4, 82.6)
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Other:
- outline, holes or cut-outs redrawn
